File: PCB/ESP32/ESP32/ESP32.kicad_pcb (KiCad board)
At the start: 2 copper layers, 49.2 x 42.5 mm, 30 parts, among them J2 USB_B_Micro, J3 Conn_01x02_Socket, J4 Conn_01x02_Pin, SW1 RESET, SW2 BOOT, SW3 LRA Switch, U1 ESP32-S2-SOLO-U-N4, U2 MCP73832T-2ACI/OT, U3 DRV2605LTDGSRQ1

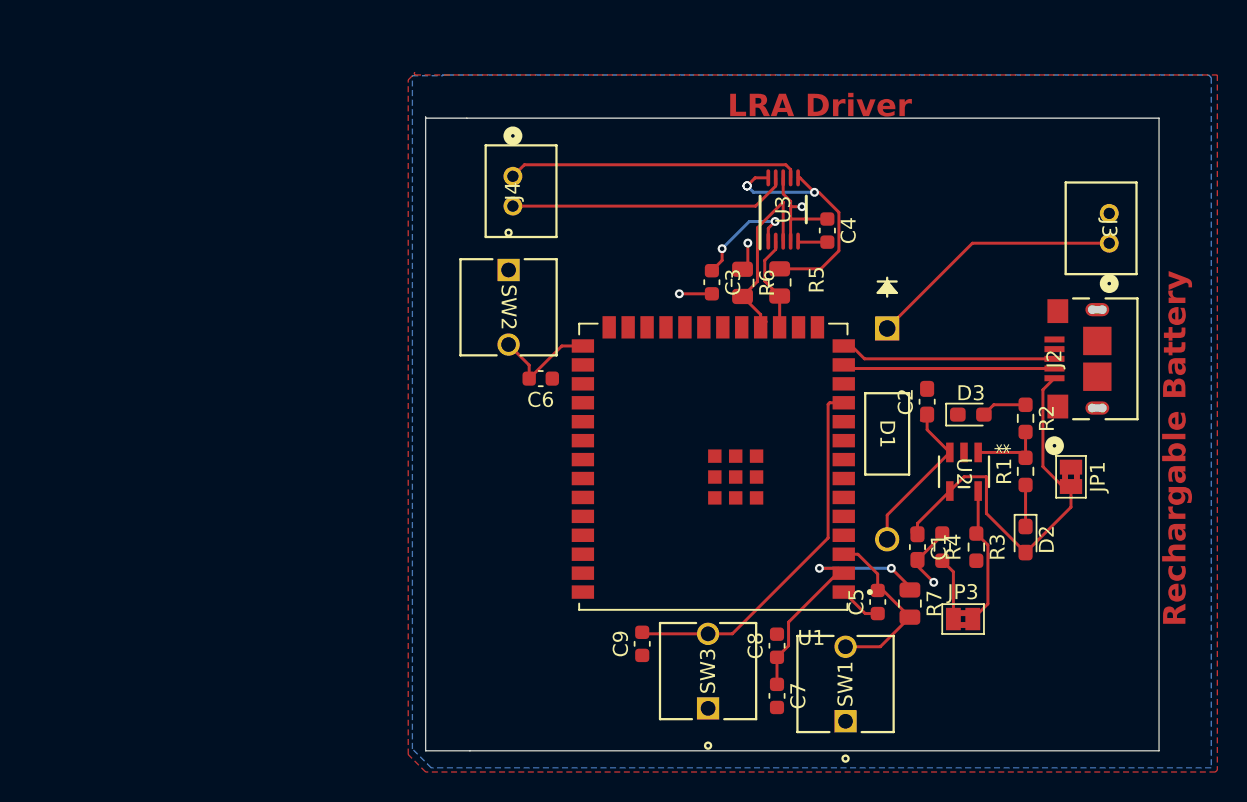
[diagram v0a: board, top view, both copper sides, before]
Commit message: New and improved footprint. Started layout
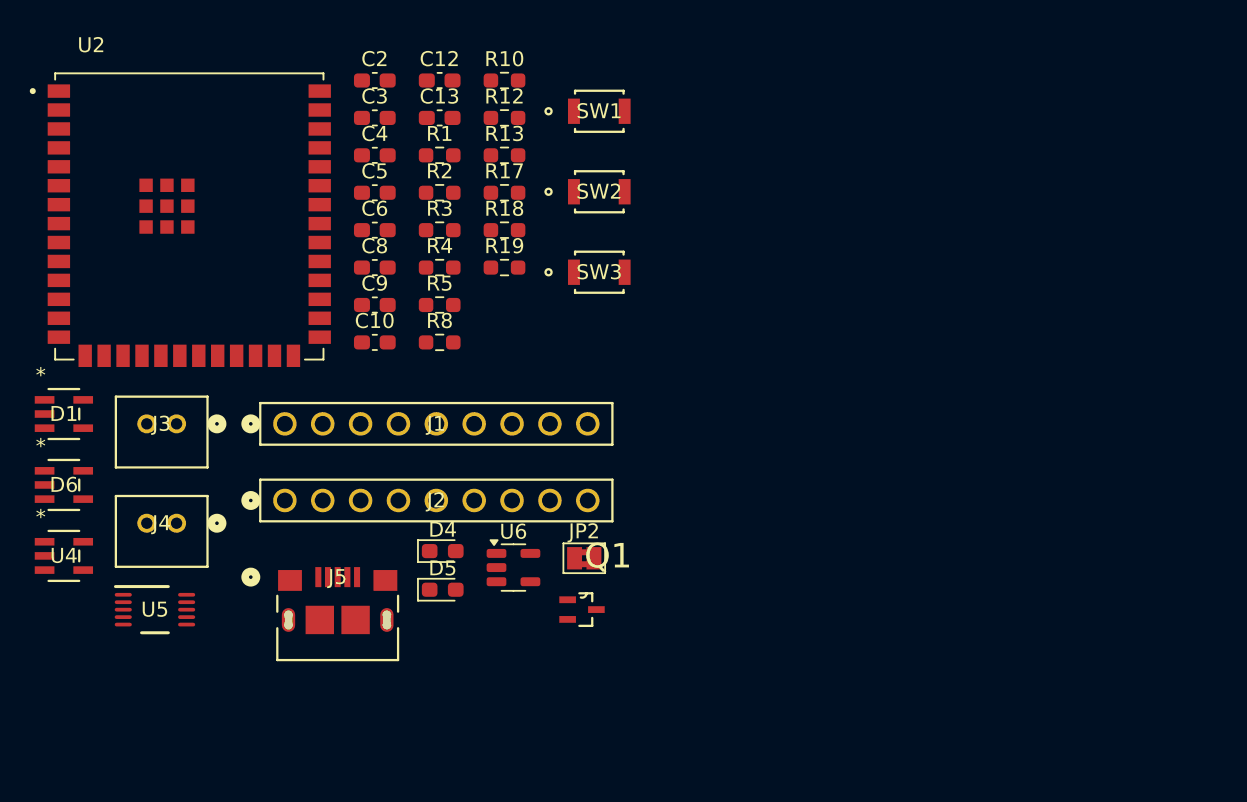
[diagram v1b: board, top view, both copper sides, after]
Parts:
- removed C1: 10μF, Capacitor_SMD:C_0603_1608Metric_Pad1.08x0.95mm_HandSolder
- removed C7: .1uF, Capacitor_SMD:C_0603_1608Metric
- removed D2, D3: LED, Diode_SMD:D_0603_1608Metric_Pad1.05x0.95mm_HandSolder
- removed JP1, JP3: SolderJumper_2_Open, Jumper:SolderJumper-2_P1.3mm_Bridged2Bar_Pad1.0x1.5mm
- removed R6: 2.2k, Resistor_SMD:R_0805_2012Metric
- removed R7: 10k, Resistor_SMD:R_0805_2012Metric
- removed U1: ESP32-S2-SOLO-U-N4, ESP32_sym_footprint:XCVR_ESP32-S2-SOLO-U-N4
- removed U3: DRV2605LTDGSRQ1, ESP32_sym_footprint:DGS0010A_L
- added C10: .1uF, Capacitor_SMD:C_0603_1608Metric_Pad1.08x0.95mm_HandSolder, F.Cu at (155.7, 93.1)
- added C12: 1uF, Capacitor_SMD:C_0603_1608Metric_Pad1.08x0.95mm_HandSolder, F.Cu at (160.1, 75.5)
- added C13: 1uF, Capacitor_SMD:C_0603_1608Metric_Pad1.08x0.95mm_HandSolder, F.Cu at (160.1, 78.0)
- added D4: LED, Diode_SMD:D_0603_1608Metric_Pad1.05x0.95mm_HandSolder, F.Cu at (160.3, 107.1)
- added D5: LED, Diode_SMD:D_0603_1608Metric_Pad1.05x0.95mm_HandSolder, F.Cu at (160.3, 109.7)
- added D6: D_Schottky, Footprint:SOT-23-5_MC_MCH, F.Cu at (134.9, 102.6)
- added J1: PPTC091LFBN-RC, Footprint:CONN9_PPTC091LFBN-RC_SUL, F.Cu at (149.7, 98.5)
- added J5: USB_B_Micro, Footprint:CONN_10118193-0001LF_AMP, F.Cu at (153.3, 111.4)
- added JP2: SolderJumper_2_Open, Jumper:SolderJumper-2_P1.3mm_Bridged2Bar_Pad1.0x1.5mm, F.Cu at (169.8, 107.6)
- added Q1: PMOS, Footprint:SOT65P210X110-3N, F.Cu at (169.6, 111.0)
- added R10: 2.2k, Resistor_SMD:R_0603_1608Metric_Pad0.98x0.95mm_HandSolder, F.Cu at (164.4, 75.5)
- added R12: 330 ohm, Resistor_SMD:R_0603_1608Metric_Pad0.98x0.95mm_HandSolder, F.Cu at (164.4, 78.0)
- added R13: 330 ohm, Resistor_SMD:R_0603_1608Metric_Pad0.98x0.95mm_HandSolder, F.Cu at (164.4, 80.5)
- added R17: 10k, Resistor_SMD:R_0603_1608Metric_Pad0.98x0.95mm_HandSolder, F.Cu at (164.4, 83.0)
- added R18: 10K, Resistor_SMD:R_0603_1608Metric_Pad0.98x0.95mm_HandSolder, F.Cu at (164.4, 85.5)
- added R19: 2.5K, Resistor_SMD:R_0603_1608Metric_Pad0.98x0.95mm_HandSolder, F.Cu at (164.4, 88.1)
- added R8: 2.2k, Resistor_SMD:R_0603_1608Metric_Pad0.98x0.95mm_HandSolder, F.Cu at (160.1, 93.1)
- added U4: MCP73832T-2ACI/OT, Footprint:SOT-23-5_MC_MCH, F.Cu at (134.9, 107.4)
- added U5: DRV2605LTDGSRQ1, Footprint:DGS0010A_L, F.Cu at (141.0, 111.0)
- added U6: AP2112K-3.3, Package_TO_SOT_SMD:SOT-23-5, F.Cu at (165.0, 108.2)
- C2: value 10μF -> .1uF
- C3, C6: footprint Capacitor_SMD:C_0603_1608Metric -> Capacitor_SMD:C_0603_1608Metric_Pad1.08x0.95mm_HandSolder
- C4: value 1uF -> .1uF; footprint Capacitor_SMD:C_0603_1608Metric -> Capacitor_SMD:C_0603_1608Metric_Pad1.08x0.95mm_HandSolder
- C5, C9: value .1uF -> 1uF; footprint Capacitor_SMD:C_0603_1608Metric -> Capacitor_SMD:C_0603_1608Metric_Pad1.08x0.95mm_HandSolder
- C8: value 1uF -> 10μF; footprint Capacitor_SMD:C_0603_1608Metric -> Capacitor_SMD:C_0603_1608Metric_Pad1.08x0.95mm_HandSolder
- D1: footprint ESP32_sym_footprint:DO-41_STM -> Footprint:SOT-23-5_MC_MCH
- J2: value USB_B_Micro -> PPTC091LFBN-RC; footprint ESP32_sym_footprint:CONN_10118193-0001LF_AMP -> Footprint:CONN9_PPTC091LFBN-RC_SUL
- J3: value Conn_01x02_Socket -> Conn_01x02_Pin; footprint ESP32_sym_footprint:CONN2_B2B-PH-K-S_JST -> Footprint:CONN2_B2B-PH-K-S_JST
- J4: value Conn_01x02_Pin -> Conn_01x02_Socket; footprint ESP32_sym_footprint:CONN2_B2B-PH-K-S_JST -> Footprint:CONN2_B2B-PH-K-S_JST
- R1: value 330 ohm -> 10k
- R2: value 330 ohm -> 4.7k
- R3: value 10K -> 10k
- R4: value 2.5K -> 4.7k
- R5: value 2.2k -> 10k; footprint Resistor_SMD:R_0805_2012Metric -> Resistor_SMD:R_0603_1608Metric_Pad0.98x0.95mm_HandSolder
- SW1, SW2, SW3: footprint ESP32_sym_footprint:SW_TL59AF160Q_EWI -> Footprint:B3U-1000P
- U2: value MCP73832T-2ACI/OT -> ESP32-S2-SOLO-U-N4; footprint ESP32_sym_footprint:SOT-23-5_MC_MCH -> Footprint:XCVR_ESP32-S2-SOLO-U-N4
- moved J3 63.7 mm to (142.4, 98.5), turned to 0 degrees
- moved D1 55.5 mm to (134.9, 97.9), turned to 0 degrees
- moved J2 55.1 mm to (149.7, 103.7), turned to 0 degrees
- moved U2 54.7 mm to (143.3, 84.6), turned to 0 degrees
- moved R1 44.7 mm to (160.1, 80.5), turned to 0 degrees
- moved SW1 44.1 mm to (170.8, 77.6), turned to 0 degrees
- moved C5 43.5 mm to (155.7, 83.0), turned to 0 degrees
- moved C2 42.9 mm to (155.7, 75.5), turned to 0 degrees
- moved R2 42.1 mm to (160.1, 83.0), turned to 0 degrees
- moved R3 41.8 mm to (160.1, 85.5), turned to 0 degrees
- moved R4 38.6 mm to (160.1, 88.1), turned to 0 degrees
- moved C8 37.0 mm to (155.7, 88.1), turned to 0 degrees
- moved J4 32.4 mm to (142.4, 105.2), turned to 0 degrees
- moved C4 30.8 mm to (155.7, 80.5), turned to 0 degrees
- moved SW3 30.2 mm to (170.8, 88.4), turned to 0 degrees
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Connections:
- C2 pad 1: Net-(D1-A) -> GND
- C2 pad 2: GND -> Net-(SW1A-B)
- C3 pad 1: Net-(U3-REG) -> GND
- C3 pad 2: GND -> Net-(SW2A-B)
- C4 pad 1: GND -> +3V3
- C4 pad 2: Net-(U3-EN) -> GND
- C5 pad 1: GND -> +3V3
- C5 pad 2: /Reset -> GND
- C6 pad 2: Net-(SW2A-B) -> Net-(SW3A-B)
- C8 pad 1: +3V3 -> Net-(J4-Pin_1)
- C9 pad 2: Net-(SW3A-B) -> Net-(U5-EN)
- J2 pad 1: Net-(D2-A) -> GND
- J2 pad 2: /USB_D- -> /SDA
- J2 pad 3: /USB_D+ -> /HS
- J2 pad 4: GND -> Net-(J2-Pad4)
- J2 pad 5: GND -> /D6
- J2 pad 6: GND -> /D4
- J2 pad 7: (no net) -> /D2
- J2 pad 8: (no net) -> /D0
- J2 pad 9: (no net) -> GND
- J3 pad 1: Net-(D1-K) -> Net-(J3-Pin_1)
- J3 pad 2: GND -> Net-(J3-Pin_2)
- J4 pad 2: Net-(J4-Pin_2) -> GND
- R1 pad 1: Net-(D2-K) -> +3V3
- R1 pad 2: Net-(R1-Pad2) -> /SDA
- R2 pad 1: Net-(D3-A) -> Net-(J2-Pad4)
- R2 pad 2: Net-(R1-Pad2) -> GND
- R3 pad 1: Net-(JP3-B) -> +3V3
- R3 pad 2: GND -> Net-(SW1A-B)
- R4 pad 1: GND -> /MCLK
- R4 pad 2: Net-(JP3-A) -> Net-(J2-Pad4)
- SW1 pad 2: /Reset -> Net-(SW1A-B)
- U2 pad 1: Net-(R1-Pad2) -> GND
- U2 pad 2: GND -> +3V3
- U2 pad 3: Net-(D1-A) -> Net-(SW1A-B)
- U2 pad 4: Net-(D2-A) -> /D3
- U2 pad 5: Net-(JP3-B) -> /D4
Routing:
- net +3V3: track 37.1 -> 0.00 mm, vias 7 -> 0
- net Net-(D2-A): track 27.5 -> 0.00 mm
- net Net-(SW3A-B): track 25.2 -> 0.00 mm
- net Net-(J4-Pin_1): track 19.6 -> 0.00 mm
- net Net-(J4-Pin_2): track 18.7 -> 0.00 mm
- net GND: track 17.6 -> 0.00 mm, vias 3 -> 0
- net Net-(D1-K): track 17.3 -> 0.00 mm
- net /USB_D+: track 14.5 -> 0.00 mm
- net /USB_D-: track 14.2 -> 0.00 mm
- net /SDA: track 13.5 -> 0.00 mm
- net /Reset: track 12.0 -> 0.00 mm
- net Net-(D1-A): track 11.4 -> 0.00 mm
- net Net-(JP3-B): track 9.38 -> 0.00 mm
- net Net-(U3-REG): track 7.58 -> 0.00 mm, vias 2 -> 0
- net Net-(SW2A-B): track 7.37 -> 0.00 mm
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- removed copper zone on B.Cu, net +3V3
- removed copper zone on F.Cu, net GND
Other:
- board size 49.2 x 42.5 mm -> 6.6 x 0.7 mm
- board text removed: "LRA Driver"
- board text removed: "Rechargable Battery"

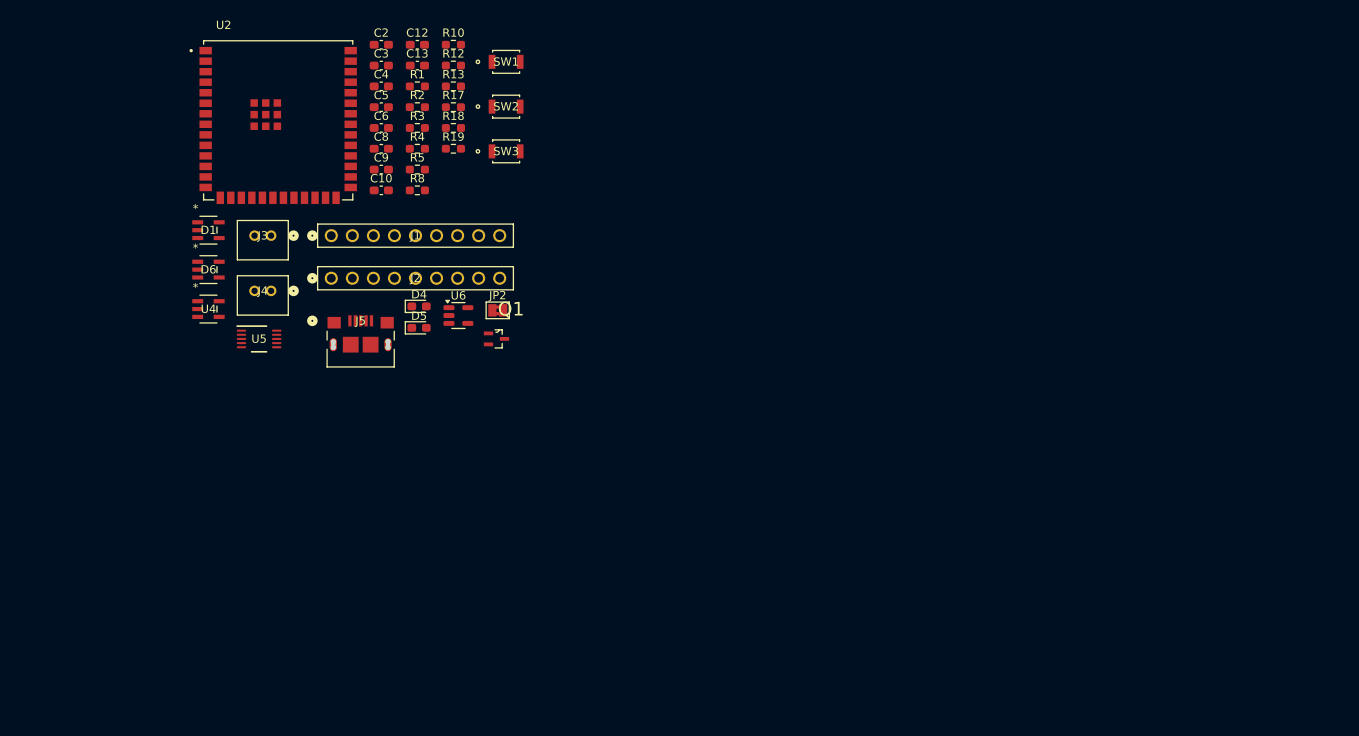
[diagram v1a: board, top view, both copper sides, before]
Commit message: Entire layout done. DRC can go-. May need to ask about edge cut errors
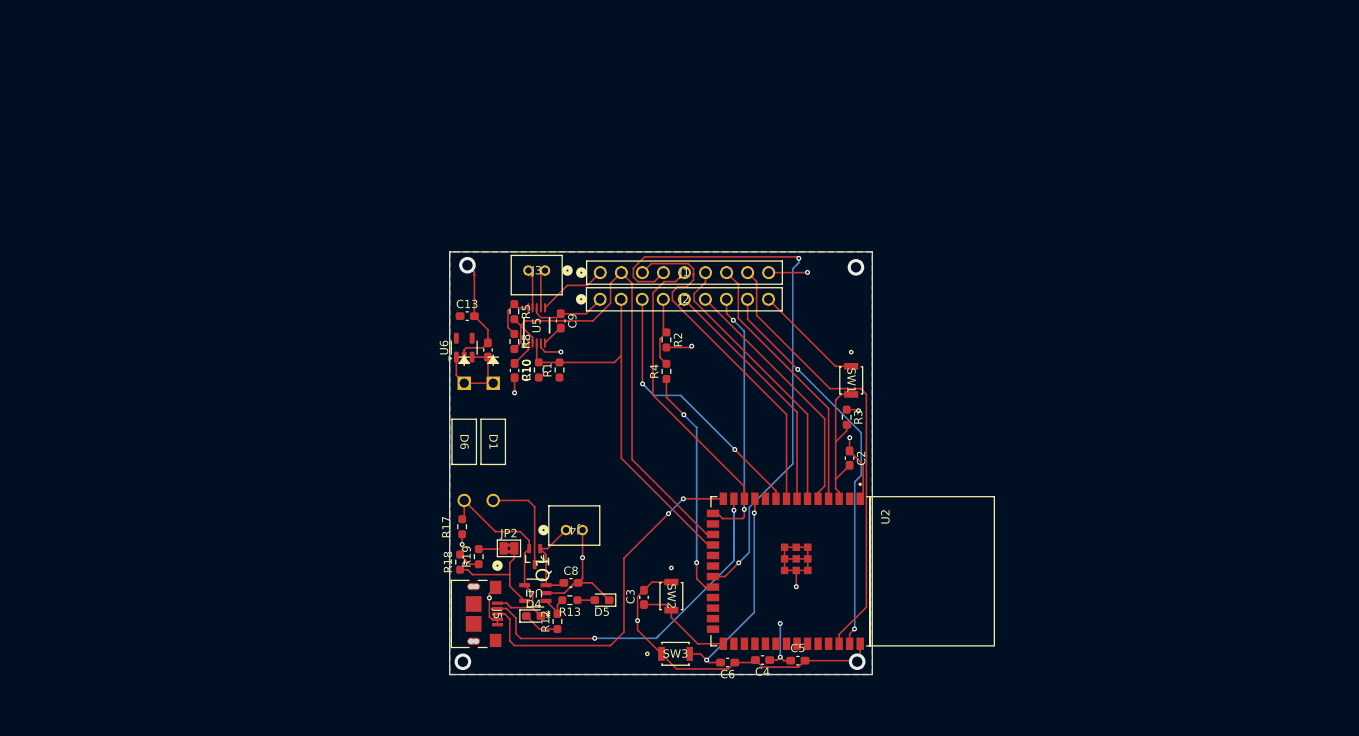
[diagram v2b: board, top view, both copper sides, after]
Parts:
- D1, D6: footprint Footprint:SOT-23-5_MC_MCH -> Footprint:DO-41_STM
- moved C5 83.6 mm to (206.0, 149.8)
- moved C4 83.1 mm to (201.8, 149.8), turned to 180 degrees
- moved U2 82.4 mm to (205.1, 139.0), turned to -90 degrees
- moved C6 76.9 mm to (197.5, 150.1), turned to 180 degrees
- moved C2 75.4 mm to (212.2, 125.4), turned to -90 degrees
- moved C3 71.6 mm to (187.4, 142.2), turned to -90 degrees
- moved R12 68.2 mm to (177.0, 145.1), turned to 90 degrees
- moved SW3 64.0 mm to (191.2, 149.0)
- moved R13 63.6 mm to (178.5, 142.5), turned to 180 degrees
- moved R3 62.5 mm to (211.9, 120.5), turned to -90 degrees
- moved SW2 62.3 mm to (190.7, 142.0), turned to -90 degrees
- moved C8 57.2 mm to (178.6, 140.4)
- moved SW1 56.7 mm to (212.4, 116.0), turned to -90 degrees
- moved R18 52.4 mm to (165.2, 137.9), turned to 90 degrees
- moved U4 52.2 mm to (174.3, 141.7), turned to 180 degrees
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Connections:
- Q1 pad 1: Net-(D1-A) -> Net-(J4-Pin_1)
- Q1 pad 3: Net-(J4-Pin_1) -> Net-(D1-A)
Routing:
- net GND: track 0.00 -> 137.4 mm, vias 0 -> 13
- net /PCLK: track 0.00 -> 69.5 mm, vias 0 -> 2
- net /SCL: track 0.00 -> 59.7 mm
- net /D1: track 0.00 -> 54.3 mm
- net /D0: track 0.00 -> 47.8 mm, vias 0 -> 2
- net /SDA: track 0.00 -> 47.3 mm
- net /USB_D+: track 0.00 -> 42.9 mm, vias 0 -> 2
- net /USB_D-: track 0.00 -> 42.8 mm, vias 0 -> 2
- net /VS: track 0.00 -> 42.3 mm
- net /D7: track 0.00 -> 34.2 mm
- net /D5: track 0.00 -> 33.5 mm
- net /HS: track 0.00 -> 32.6 mm, vias 0 -> 2
- net /D3: track 0.00 -> 32.4 mm
- net /D2: track 0.00 -> 31.2 mm, vias 0 -> 2
- net /D4: track 0.00 -> 30.3 mm
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- added copper zone on F.Cu, net +3V3
- added copper zone on B.Cu, net GND
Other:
- board size 6.6 x 0.7 mm -> 51 x 51 mm

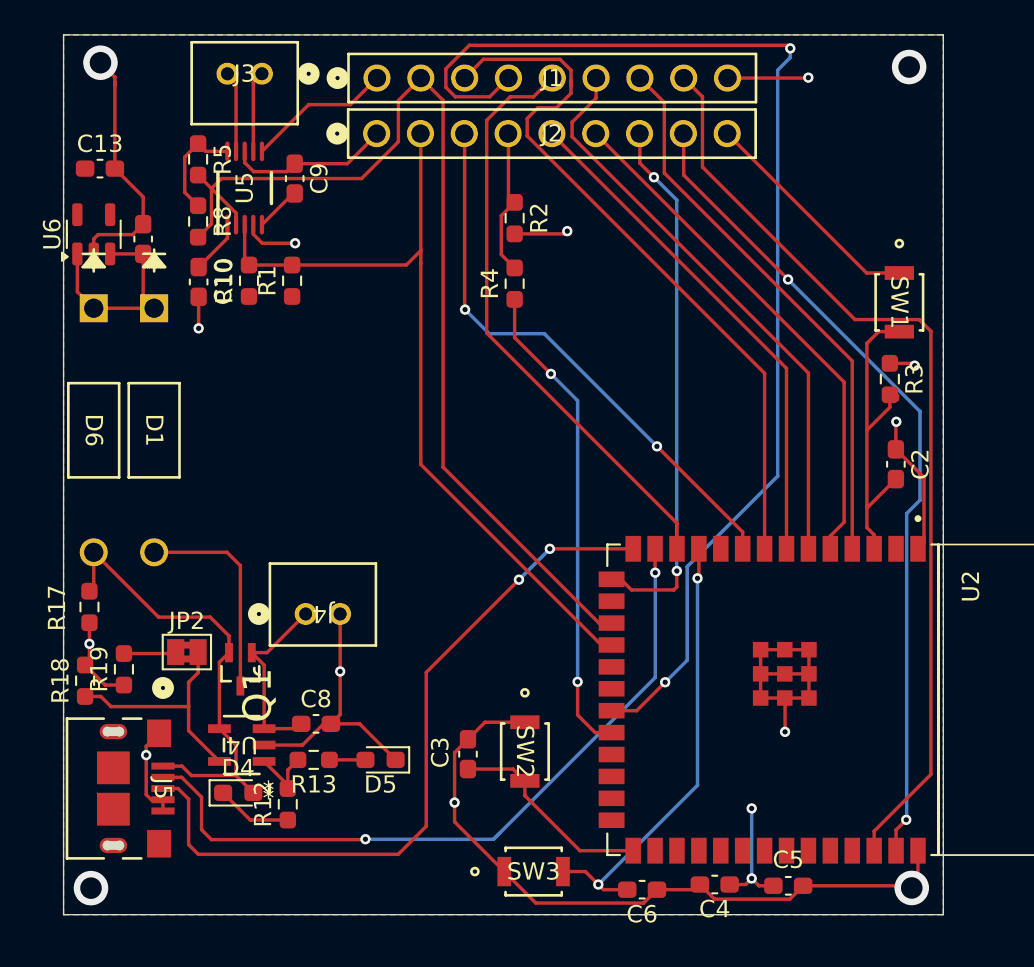
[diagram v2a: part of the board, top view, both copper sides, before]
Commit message: Fixes
Fixed 3v3 net, added labels for different bus voltages, cleaned up silkscreen.
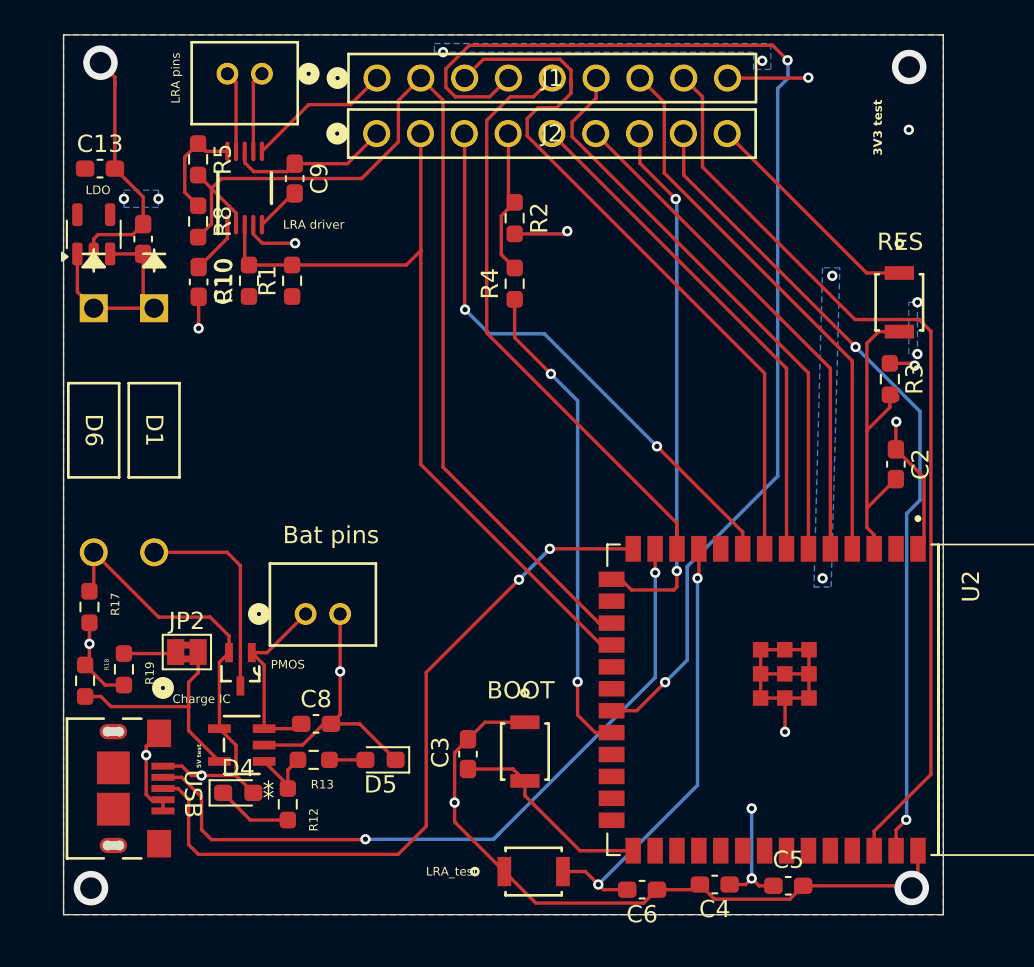
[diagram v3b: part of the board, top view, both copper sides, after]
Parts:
- Bat pins: renamed from J4
- Charge IC: renamed from U4
- LRA driver: renamed from U5
- LRA pins: renamed from J3
- renumbered SW2 to BOOT, U6 to LDO, SW3 to LRA_test, Q1 to PMOS, SW1 to RES, J5 to USB
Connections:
- net Net-(D4-A) renamed 5V
- net Net-(J4-Pin_1) renamed Charge-line
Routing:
- net /D4: track 30.3 -> 29.7 mm
- net /PCLK: track 69.5 -> 68.9 mm
- net 5V: vias 0 -> 1
- net +3V3: vias 4 -> 13
- added copper zone on B.Cu, net +3V3
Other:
- board text added: "3V3 test"
- board text added: "5V test"
